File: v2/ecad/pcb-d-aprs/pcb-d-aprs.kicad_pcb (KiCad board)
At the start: 4 copper layers, 80 x 62 mm, 100 parts, among them Q1 BC847 (PTT2, spare), Q2 BC847 (PTT to the module), Q3 2N7002 (EMCON inhibit in Q2 e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, Q4 BC857 (TR mirror from RADIO_P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, U1 TPS61089 boost 7.6 V / 2 A, U2 DNP bench: DMR858M 5 W UHF mo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, U3 AP2112K-3.3 digital, U4 AP2112K-3.3 analog, U5 STM32F302CBT6 128 KB (AIOC fi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, U6 USBLC6-2SC6, Y1 8MHz 20pF 5032

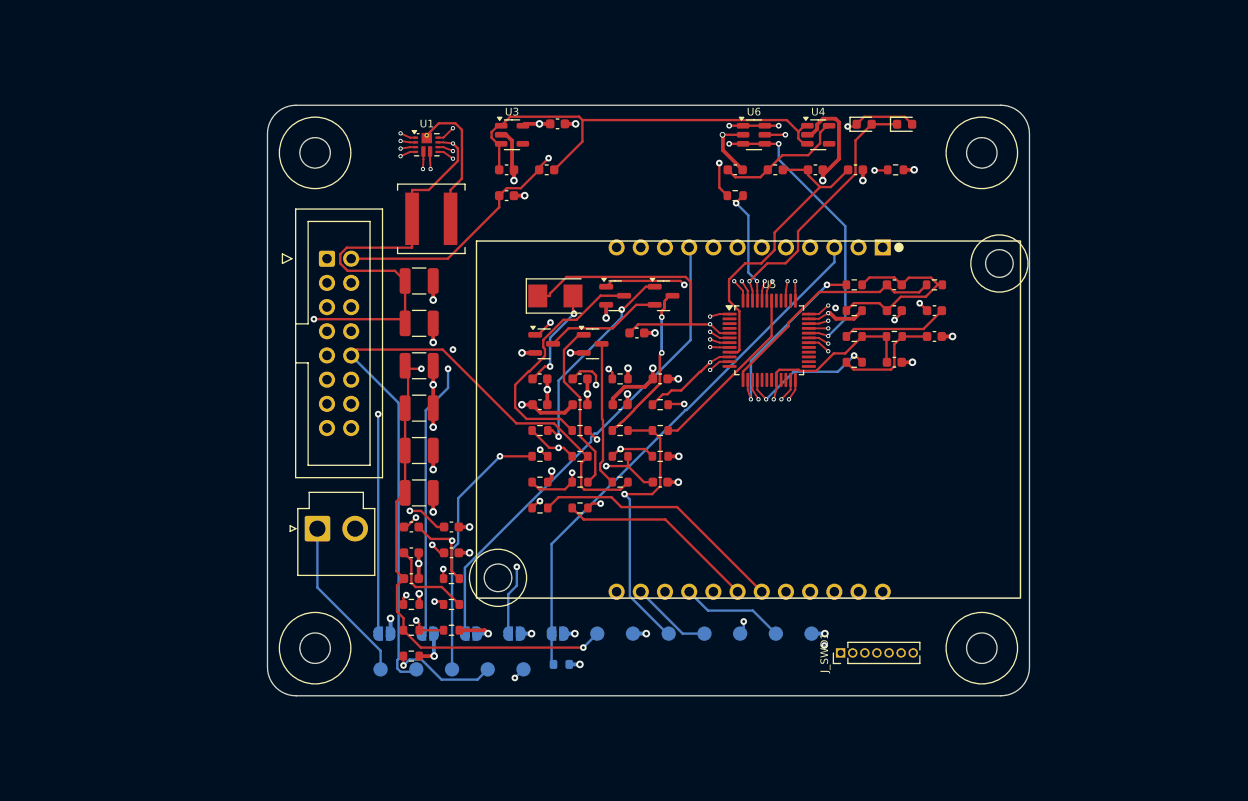
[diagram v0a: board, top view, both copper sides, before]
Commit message: feat(pcb-a,pcb-d): A20 and D6 routed and finished on the laptop [MESHSAT-795]
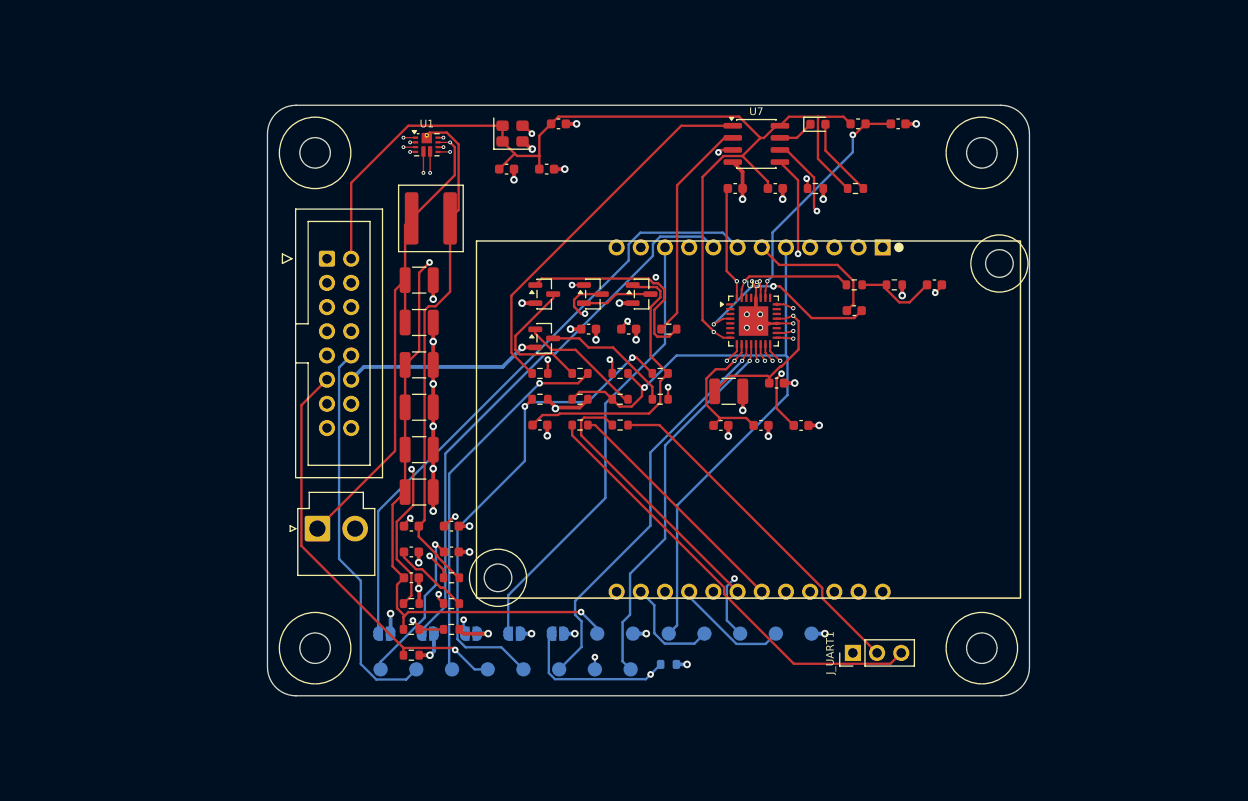
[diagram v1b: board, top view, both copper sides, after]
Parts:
- removed C1, C2: 22p NP0, C_0603_1608Metric
- removed C11: 4.7n NP0, C_0603_1608Metric
- removed C12, C15, C16: 100n, C_0603_1608Metric
- removed C31, C4, C5, C6: 4.7u, C_0603_1608Metric
- removed D2: red, LED_0603_1608Metric
- removed FB2: 600R@100MHz, L_0603_1608Metric
- removed J_SWD1: SWD/DFU 1.27 mm: BOOT0 SWO NRST SWDIO GND SWCLK 3V3 (short 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, PinHeader_1x07_P1.27mm_Vertical
- removed R1, R18, R19: 1.5k, R_0603_1608Metric
- removed R14, R16, R5: 5.1k, R_0603_1608Metric
- removed R17: 100R, R_0603_1608Metric
- removed R22: DNP 100R (mirror now via Q4), R_0603_1608Metric
- removed U3: AP2112K-3.3 digital, SOT-23-5
- removed U4: AP2112K-3.3 analog, SOT-23-5
- removed U6: USBLC6-2SC6, SOT-23-6
- removed Y1: 8MHz 20pF 5032, Crystal_SMD_5032-2Pin_5.0x3.2mm
- added C33: 100n, C_0603_1608Metric, F.Cu at (113.5, 98.2)
- added C34: 10u, C_1210_3225Metric, F.Cu at (108.4, 99.0)
- added C35: 100n, C_0603_1608Metric, F.Cu at (107.6, 102.6)
- added C36: 100n, C_0603_1608Metric, F.Cu at (111.8, 102.6)
- added C37: 4.7u, C_0603_1608Metric, F.Cu at (116.0, 102.6)
- added C38: 100n, C_0603_1608Metric, F.Cu at (90.6, 71.0)
- added C39: 100n, C_0603_1608Metric, F.Cu at (113.3, 77.7)
- added J_UART1: DMR858M host-upgrade UART (bench, 3.3 V, 100R in series): G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, PinHeader_1x03_P2.54mm_Vertical, F.Cu at (121.5, 126.5)
- added TP13: MCLK, TestPoint_Pad_D1.5mm, B.Cu at (90.6, 128.2)
- added TP14: +3V3_AB, TestPoint_Pad_D1.5mm, B.Cu at (94.4, 128.2)
- added TP15: I2S_BCLK, TestPoint_Pad_D1.5mm, B.Cu at (98.1, 128.2)
- added U7: PCA9536 4-bit I2C expander 0x41: 0 PTT, 1 PTT2 (spare), 2 S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, SOIC-8_3.9x4.9mm_P1.27mm, F.Cu at (111.3, 73.1)
- added X1: 24 MHz 3.3 V oscillator 3225 (ASE-24.000MHZ-LC-T class), Oscillator_SMD_Abracon_ASE-4Pin_3.2x2.5mm, F.Cu at (85.7, 72.0)
- D1: value green -> green status (U7 bit 3 sinks)
- J_HARN1: value harness to PCB-A J_MEZZ1 (IDC 2x8); UART pair and PCB-A 3V3 unused -> harness to PCB-A J_MEZZ1 (IDC 2x8): I2S, I2C, the gated 3.3 V from B13, PTT lines
- R15: value 100R -> 1k
- R3: value 100R -> 100k
- U5: value STM32F302CBT6 128 KB (AIOC firmware 1.4.1 is 128,016 bytes; DFU) -> WM8960 audio codec QFN-32 (pins per datasheet table: 4 LINPUT1, 11 MCLK, 12 BCLK, 13 DACLRC, 14 DACDAT, 15 ADCLRC, 16 A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; footprint LQFP-48_7x7mm_P0.5mm -> QFN-32-1EP_5x5mm_P0.5mm_EP3.1x3.1mm
- moved C7 27.3 mm to (85.1, 75.7)
- moved C8 24.7 mm to (89.3, 75.7)
- moved R3 18.7 mm to (117.5, 77.7)
- moved R38 14.0 mm to (88.6, 99.9)
- moved C32 14.0 mm to (88.6, 102.6)
- moved C10 12.8 mm to (109.1, 77.7)
- moved R15 12.7 mm to (121.7, 77.7)
- moved Q3 11.5 mm to (99.3, 88.8)
- moved R36 11.2 mm to (102.1, 127.7)
- moved C9 9.94 mm to (126.2, 71.0)
- moved FB1 9.94 mm to (122.0, 71.0)
- moved R40 9.67 mm to (97.0, 99.9)
- moved R9 9.67 mm to (97.0, 102.6)
- moved R37 9.67 mm to (101.2, 97.2)
- moved R39 9.67 mm to (92.8, 99.9)
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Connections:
- C14 pad 2: /SPK_NODE -> /SPK_IN
- C18 pad 1: +3V3 -> /+3V3_AB
- C7 pad 1: +3V3 -> /+3V3_AB
- C8 pad 1: +3V3 -> /+3V3_AB
- FB1 pad 1: /LDO_A -> /+3V3_AB
- J_HARN1 pad 12: (no net) -> +3V3
- J_HARN1 pad 14: /SPKEN -> /SCL
- J_HARN1 pad 2: /+5V_USB -> /+3V3_AB
- J_HARN1 pad 3: /USB_DP -> /I2S_BCLK
- J_HARN1 pad 4: /USB_DM -> /I2S_LRCLK
- J_HARN1 pad 6: (no net) -> /I2S_DOUT
- J_HARN1 pad 7: (no net) -> /I2S_DIN
- J_HARN1 pad 8: (no net) -> GND
- J_HARN1 pad 9: GND -> /SDA
- R15 pad 1: /LED_K -> /+3V3_AB
- R15 pad 2: /LED_R -> /LED_A
- R3 pad 1: /BIAS_NODE -> /SPKEN
- R3 pad 2: /ADC_BIAS -> GND
- R8 pad 1: /USART_TX -> /UART_TX_H
- R9 pad 2: /USART_RX -> /UART_RX_H
- U5 pad 1: +3V3 -> (no net)
- U5 pad 10: /OUT2 -> /+3V3_AB
- U5 pad 11: /OUT1 -> /MCLK
- U5 pad 12: (no net) -> /I2S_BCLK
- U5 pad 13: /DAC_ATTEN -> /I2S_LRCLK
- U5 pad 14: /AFOUT -> /I2S_DOUT
- U5 pad 15: /AFIN -> /I2S_LRCLK
- U5 pad 16: /ADC_BIAS -> /I2S_DIN
- U5 pad 17: (no net) -> /SCL
- U5 pad 18: (no net) -> /SDA
- U5 pad 20: /AFIN -> GND
- U5 pad 21: (no net) -> /+3.3VA
- U5 pad 23: GND -> (no net)
- U5 pad 24: +3V3 -> GND
- U5 pad 26: (no net) -> /+3.3VA
- U5 pad 27: (no net) -> /VMID
- U5 pad 28: (no net) -> GND
- U5 pad 30: /USART_TX -> (no net)
- U5 pad 31: /USART_RX -> /AFOUT
- U5 pad 32: /USB_DM -> /+3.3VA
- U5 pad 33: /USB_DP -> GND
- U5 pad 4: (no net) -> /SPK_IN
- U5 pad 5: /OSCIN -> (no net)
- U5 pad 6: /OSCOUT -> (no net)
- U5 pad 7: /NRST -> (no net)
- U5 pad 8: GND -> /+3V3_AB
- U5 pad 9: /+3.3VA -> GND
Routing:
- net /+3V3_AB: track 0.00 -> 181.8 mm, vias 0 -> 4
- net +3V3: track 216.5 -> 91.3 mm, vias 13 -> 5
- net /USB_DP: track 91.7 -> 0.00 mm, vias 4 -> 0
- net /I2S_BCLK: track 0.00 -> 88.2 mm, vias 0 -> 1
- net /USB_DM: track 79.9 -> 0.00 mm, vias 3 -> 0
- net /MCLK: track 0.00 -> 78.3 mm, vias 0 -> 3
- net /SCL: track 0.00 -> 76.2 mm, vias 0 -> 2
- net /BOOT0: track 76.0 -> 0.00 mm, vias 2 -> 0
- net /SDA: track 0.00 -> 75.3 mm, vias 0 -> 2
- net /NRST: track 62.1 -> 0.00 mm, vias 3 -> 0
- net GND: track 436.2 -> 375.1 mm, vias 38 -> 44
- net /+5V_USB: track 54.0 -> 0.00 mm, vias 2 -> 0
- net /I2S_LRCLK: track 0.00 -> 53.0 mm, vias 0 -> 2
- net /I2S_DIN: track 0.00 -> 52.1 mm, vias 0 -> 1
- net /I2S_DOUT: track 0.00 -> 48.4 mm, vias 0 -> 1
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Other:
- board text added: "N: D6 core (top clock/expander/LED, bottom codec/audio/PTT)"
- board text removed: "N: core (top LDO/USB/LED/SWD, bottom MCU/audio/PTT)"

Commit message: feat(pcb-a,pcb-d): A20 and D6 routed and finished (fix round) [MESHSAT-795]
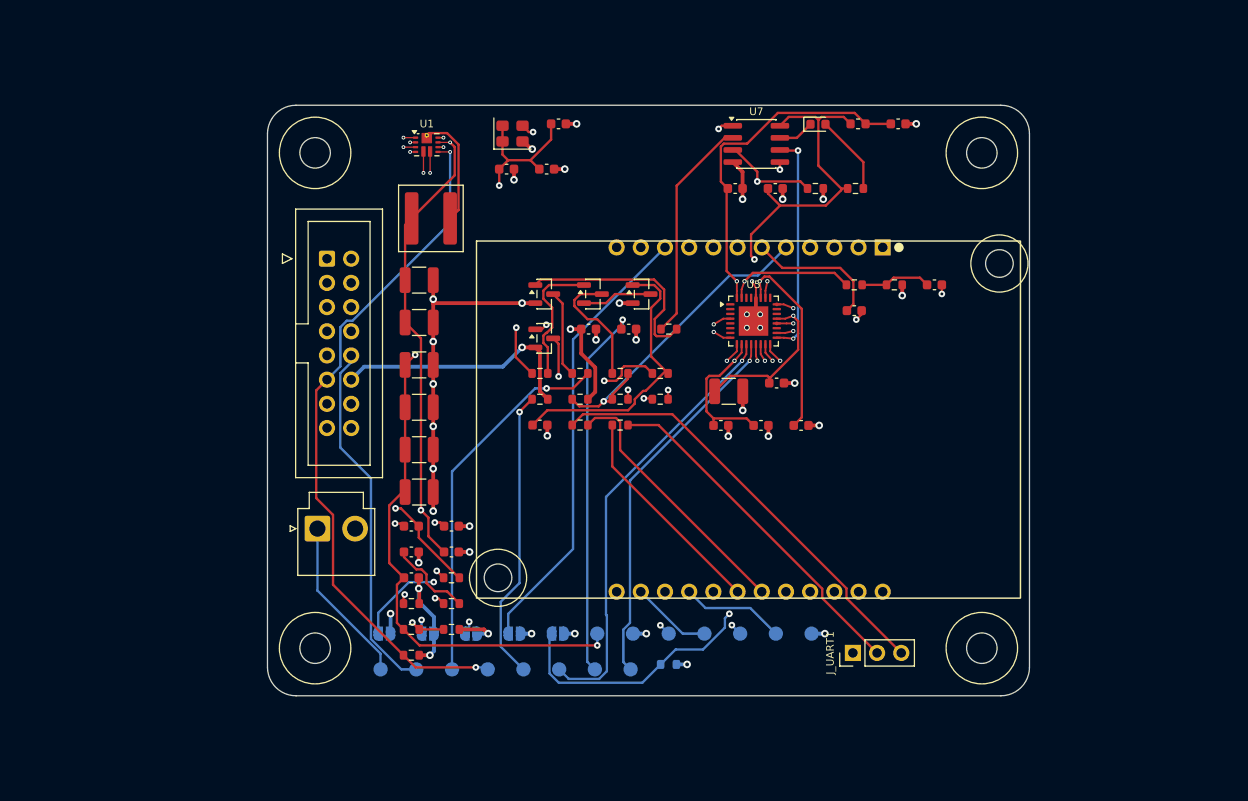
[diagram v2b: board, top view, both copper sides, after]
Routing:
- net /MCLK: track 78.3 -> 98.4 mm, vias 3 -> 2
- net /+3V3_AB: track 181.8 -> 168.0 mm, vias 4 -> 5
- net /RADIO_PTT: track 74.0 -> 61.3 mm, vias 1 -> 2
- net /SW: track 53.7 -> 63.3 mm, vias 0 -> 1
- net +3V3: track 91.3 -> 100.0 mm, vias 5 -> 4
- net /TX_INHIBIT_n: track 74.6 -> 68.3 mm
- net /FB8: track 65.2 -> 59.0 mm
- net /VIN_CELL: track 83.7 -> 77.6 mm
- net GND: track 375.1 -> 369.2 mm
- net /RADIO_TX: track 28.5 -> 22.9 mm
- net /Q1_C: track 14.5 -> 9.16 mm
- net /SPKEN: track 71.5 -> 67.1 mm, vias 2 -> 1
- net /TR_APRS: track 76.7 -> 73.4 mm
- net /CH8: track 64.3 -> 67.5 mm, vias 0 -> 1
- net /ILIM: track 53.2 -> 50.2 mm
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
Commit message: feat(pcb-d): D6 routed and finished at the 0.14 mm rule [MESHSAT-795]
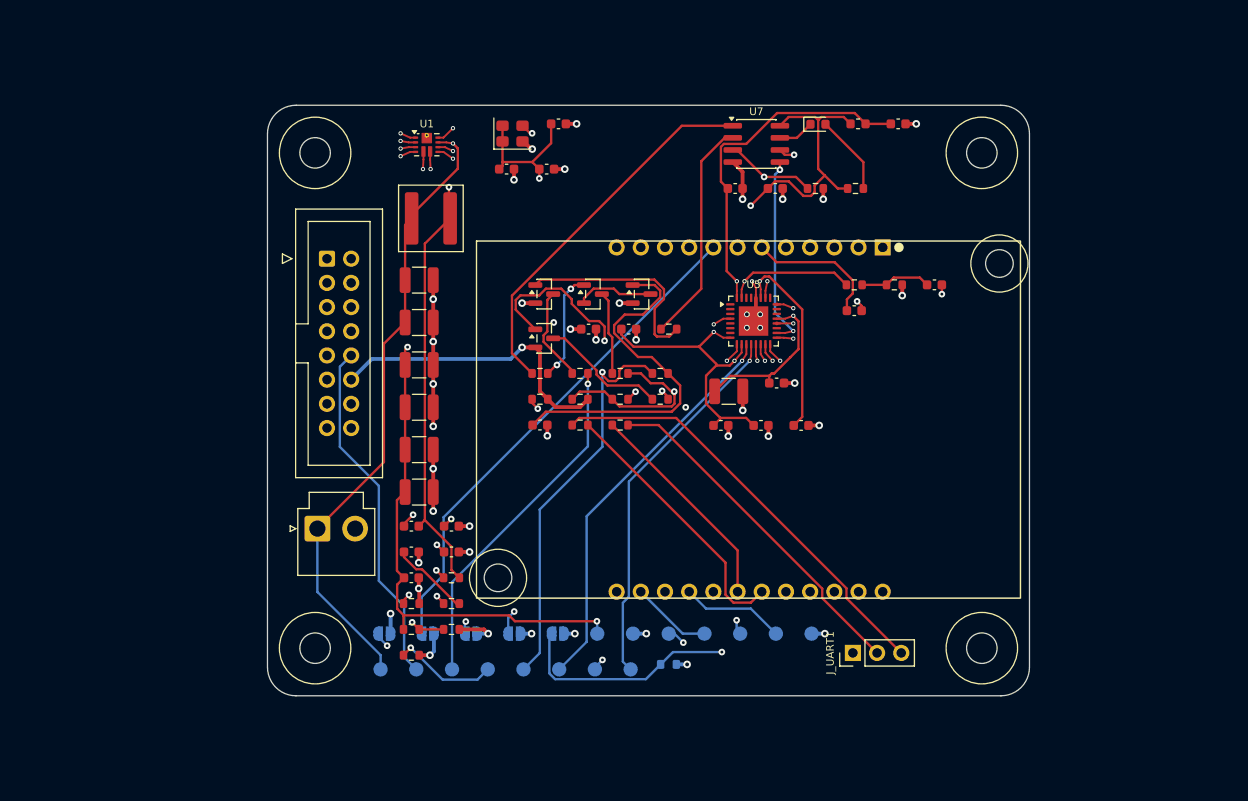
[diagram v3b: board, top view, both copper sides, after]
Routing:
- net /+3V3_AB: track 168.0 -> 183.5 mm
- net /MCLK: track 98.4 -> 85.8 mm, vias 2 -> 3
- net /RADIO_PTT: track 61.3 -> 73.7 mm
- net /Q4_B: track 14.7 -> 25.0 mm
- net /SW: track 63.3 -> 53.0 mm
- net /Q3_G: track 29.5 -> 38.2 mm
- net /CH4: track 61.0 -> 53.2 mm, vias 1 -> 0
- net GND: track 369.2 -> 377.0 mm
- net /FB8: track 59.0 -> 66.1 mm
- net /TX_INHIBIT_n: track 68.3 -> 74.4 mm
- net /COMP: track 58.1 -> 64.1 mm
- net /CH8: track 67.5 -> 62.4 mm, vias 1 -> 2
- net /Q2_C: track 13.1 -> 8.78 mm
- net /BST_VCC: track 48.3 -> 52.1 mm
- net /SPKEN: track 67.1 -> 70.7 mm
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
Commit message: feat(pcb-d): D7 routed and finished for the DMR858M V1.0 board [MESHSAT-804]
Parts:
- removed JP1: channel bit CH8 to GND (open = default), SolderJumper-2_P1.3mm_Open_RoundedPad1.0x1.5mm
- removed JP2: channel bit CH4 to GND (open = default), SolderJumper-2_P1.3mm_Open_RoundedPad1.0x1.5mm
- removed JP3: channel bit CH2 to GND (open = default), SolderJumper-2_P1.3mm_Open_RoundedPad1.0x1.5mm
- removed JP4: channel bit CH1 to GND (open = default), SolderJumper-2_P1.3mm_Open_RoundedPad1.0x1.5mm
- removed JP5: CS to GND = module sleep, SolderJumper-2_P1.3mm_Open_RoundedPad1.0x1.5mm
- removed J_UART1: DMR858M host-upgrade UART (bench, 3.3 V, 100R in series): G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, PinHeader_1x03_P2.54mm_Vertical
- added C40: 100n, C_0603_1608Metric, F.Cu at (97.0, 107.4)
- added R42: 1k, R_0603_1608Metric, F.Cu at (125.8, 90.6)
- added R43: 1k, R_0603_1608Metric, F.Cu at (130.0, 90.6)
- added R44: 1k, R_0603_1608Metric, F.Cu at (121.6, 93.3)
- added R45: 1k, R_0603_1608Metric, F.Cu at (125.8, 93.3)
- added R46: 1k, R_0603_1608Metric, F.Cu at (130.0, 93.3)
- added R47: 10k, R_0603_1608Metric, F.Cu at (101.2, 107.4)
- added R48: 1k, R_0603_1608Metric, F.Cu at (121.6, 96.0)
- added R49: 100k, R_0603_1608Metric, B.Cu at (83.8, 127.7)
- added R50: 100k, R_0603_1608Metric, B.Cu at (88.0, 127.7)
- added R51: 100k, R_0603_1608Metric, B.Cu at (92.2, 127.7)
- added R52: 100k, R_0603_1608Metric, B.Cu at (96.4, 127.7)
- added U8: SC16IS740IPW I2C-to-UART bridge 0x48, 24 MHz external clock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, TSSOP-16_4.4x5mm_P0.65mm, F.Cu at (92.8, 89.9)
- R2: value 4.7k -> 47k
- R4: value 1.5k -> 1k
- TP6: value SPKEN -> RADIO_COS
- U7: value PCA9536 4-bit I2C expander 0x41: 0 PTT, 1 PTT2 (spare), 2 SPKEN, 3 status LED; a gpiochip for Direwolf's PTT -> PCA9555PW 0x26: PTT, PTT2, LED, CS, COS in, channel code in; footprint SOIC-8_3.9x4.9mm_P1.27mm -> TSSOP-24_4.4x7.8mm_P0.65mm
- moved TP10 26.5 mm to (105.6, 124.5)
- moved TP11 26.5 mm to (109.4, 124.5)
- moved TP12 26.5 mm to (113.1, 124.5)
- moved TP13 26.5 mm to (116.9, 124.5)
- moved TP8 26.5 mm to (98.1, 124.5)
- moved TP9 26.5 mm to (101.9, 124.5)
- moved TP1 22.8 mm to (71.9, 124.5)
- moved TP2 22.8 mm to (75.6, 124.5)
- moved TP3 22.8 mm to (79.4, 124.5)
- moved TP4 22.8 mm to (83.1, 124.5)
- moved TP5 22.8 mm to (86.9, 124.5)
- moved TP6 22.8 mm to (90.6, 124.5)
- moved TP7 22.8 mm to (94.4, 124.5)
- moved R36 22.5 mm to (79.6, 127.7)
- moved TP14 22.5 mm to (71.9, 128.2)
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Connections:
- R3 pad 1: /SPKEN -> /RADIO_COS
- R36 pad 2: +3V3 -> /+3V3_AB
- R8 pad 1: /UART_TX_H -> /BR_TX
- R9 pad 2: /UART_RX_H -> /BR_RX
- TP6 pad 1: /SPKEN -> /RADIO_COS
- U2 pad 16: /SPKEN -> /RADIO_COS
- U7 pad 1: /OUT1 -> (no net)
- U7 pad 2: /OUT2 -> /+3V3_AB
- U7 pad 3: /SPKEN -> /+3V3_AB
- U7 pad 4: GND -> /OUT1
- U7 pad 5: /SDA -> /OUT2
- U7 pad 6: /SCL -> /LED_K
- U7 pad 7: /LED_K -> /CS_CTL
- U7 pad 8: /+3V3_AB -> /RADIO_COS_IN
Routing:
- net /CH8_IN: track 0.00 -> 95.7 mm, vias 0 -> 2
- net /V8: track 128.1 -> 36.9 mm, vias 3 -> 2
- net /CH1_IN: track 0.00 -> 90.5 mm, vias 0 -> 3
- net /CH2_IN: track 0.00 -> 84.9 mm, vias 0 -> 3
- net /CH4_IN: track 0.00 -> 83.9 mm, vias 0 -> 2
- net /RADIO_COS: track 0.00 -> 77.9 mm, vias 0 -> 3
- net /SPKEN: track 70.7 -> 0.00 mm, vias 1 -> 0
- net /+3V3_AB: track 183.5 -> 230.1 mm, vias 5 -> 12
- net /UART_TX_H: track 45.7 -> 0.00 mm
- net /CH8: track 62.4 -> 23.9 mm, vias 2 -> 1
- net /UART_RX_H: track 36.6 -> 0.00 mm
- net /CH4: track 53.2 -> 17.8 mm
- net /CS_CTL: track 0.00 -> 32.4 mm, vias 0 -> 2
- net /CH2: track 54.8 -> 25.2 mm
- net /BR_TX: track 0.00 -> 27.1 mm, vias 0 -> 2
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- added copper zone on B.Cu, net V8
- added copper zone on B.Cu, net VIN_CELL
